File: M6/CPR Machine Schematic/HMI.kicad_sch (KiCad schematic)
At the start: 0 parts

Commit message: morer kicad
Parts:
- added J2: Raspberry_Pi_4, symbol Connector:Raspberry_Pi_4
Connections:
- new net: J2.1 (3V3), J2.17 (3V3)
- new net: J2.14 (GND), J2.20 (GND), J2.25 (GND), J2.30 (GND), J2.34 (GND), J2.39 (GND), J2.6 (GND), J2.9 (GND)
- new net +5V: J2.2 (5V), J2.4 (5V)
- new net UART_RX: J2.10 (GPIO15/UART_RXD)
- new net UART_TX: J2.8 (GPIO14/UART_TXD)
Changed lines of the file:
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@@
 	(generator_version "9.0")
 	(paper "A4")
+	(hierarchical_label "UART_TX"
+		(shape output)
+		(at 48.26 68.58 180)
+		(effects
+			(font
+				(size 1.27 1.27)
+			)
+			(justify right)
+		)
+	)
+	(hierarchical_label "UART_RX"
+		(shape input)
+		(at 48.26 71.12 180)
+		(effects
+			(font
+				(size 1.27 1.27)
+			)
+			(justify right)
+		)
+	)
+	(symbol
+		(lib_id "power:+5V")
+		(at 114.3 60.96 270)
+		(unit 1)
+		(exclude_from_sim no)
+		(in_bom yes)
+		(on_board yes)
+		(dnp no)
+		(fields_autoplaced yes)
+		(property "Reference" "#PWR02"
+			(at 110.49 60.96 0)
+			(effects
+				(font
+					(size 1.27 1.27)
+				)
+				(hide yes)
+			)
+		)
+		(property "Value" "+5V"
+			(at 118.11 60.9599 90)
+			(effects
+				(font
+					(size 1.27 1.27)
+				)
+				(justify left)
+			)
+		)
+		(property "Footprint" ""
+			(at 114.3 60.96 0)
+			(effects
+				(font
+					(size 1.27 1.27)
+				)
+				(hide yes)
+			)
+		)
+		(property "Datasheet" ""
+			(at 114.3 60.96 0)
+			(effects
+				(font
+					(size 1.27 1.27)
+				)
+				(hide yes)
+			)
+		)
+		(property "Description" "Power symbol creates a global label with name \"+5V\""
+			(at 114.3 60.96 0)
+			(effects
+				(font
+					(size 1.27 1.27)
+				)
+				(hide yes)
+			)
+		)
+		(pin "1"
+		)
+		(instances
+			(project ""
+				(path "/8991fc77-975f-4978-a089-6b2a5e33f59b/6f4ed3f2-e76d-4623-90c5-067eb820b8e2"
+					(reference "#PWR02")
+					(unit 1)
+				)
+			)
+		)
+	)
+	(symbol
+		(lib_id "Connector:Raspberry_Pi_4")
+		(at 81.28 83.82 0)
+		(unit 1)
+		(exclude_from_sim no)
+		(in_bom yes)
+		(on_board yes)
+		(dnp no)
+		(fields_autoplaced yes)
+		(property "Reference" "J2"
+			(at 81.28 53.34 0)
+			(effects
+				(font
+					(size 1.27 1.27)
+				)
+			)
+		)
+		(property "Value" "Raspberry_Pi_4"
+			(at 81.28 55.88 0)
+			(effects
+				(font
+					(size 1.27 1.27)
+				)
+			)
+		)
+		(property "Footprint" ""
+			(at 151.384 131.318 0)
+			(effects
+				(font
+					(size 1.27 1.27)
+				)
+				(justify left)
+				(hide yes)
+			)
+		)
+		(property "Datasheet" "https://datasheets.raspberrypi.com/rpi4/raspberry-pi-4-datasheet.pdf"
+			(at 97.028 116.078 0)
+			(effects
+				(font
+					(size 1.27 1.27)
+				)
+				(justify left)
+				(hide yes)
+			)
+		)
+		(property "Description" "Raspberry Pi 4 Model B"
+			(at 97.028 113.538 0)
+			(effects
+				(font
+					(size 1.27 1.27)
+				)
+				(justify left)
+				(hide yes)
+			)
+		)
+		(pin "32"
+		)
+		(pin "33"
+		)
+		(pin "35"
+		)
+		(pin "22"
+		)
+		(pin "20"
+		)
+		(pin "25"
+		)
+		(pin "30"
+		)
+		(pin "8"
+		)
+		(pin "6"
+		)
+		(pin "40"
+		)
+		(pin "12"
+		)
+		(pin "14"
+		)
+		(pin "13"
+		)
+		(pin "36"
+		)
+		(pin "38"
+		)
+		(pin "10"
+		)
+		(pin "15"
+		)
+		(pin "34"
+		)
+		(pin "16"
+		)
+		(pin "18"
+		)
+		(pin "39"
+		)
+		(pin "37"
+		)
+		(pin "11"
+		)
+		(pin "31"
+		)
+		(pin "5"
+		)
+		(pin "9"
+		)
+		(pin "17"
+		)
+		(pin "1"
+		)
+		(pin "21"
+		)
+		(pin "19"
+		)
+		(pin "27"
+		)
+		(pin "7"
+		)
+		(pin "4"
+		)
+		(pin "29"
+		)
+		(pin "23"
+		)
+		(pin "3"
+		)
+		(pin "2"
+		)
+		(pin "28"
+		)
+		(pin "26"
+		)
+		(pin "24"
+		)
+		(instances
+			(project ""
+				(path "/8991fc77-975f-4978-a089-6b2a5e33f59b/6f4ed3f2-e76d-4623-90c5-067eb820b8e2"
+					(reference "J2")
+					(unit 1)
+				)
+			)
+		)
+	)
 )

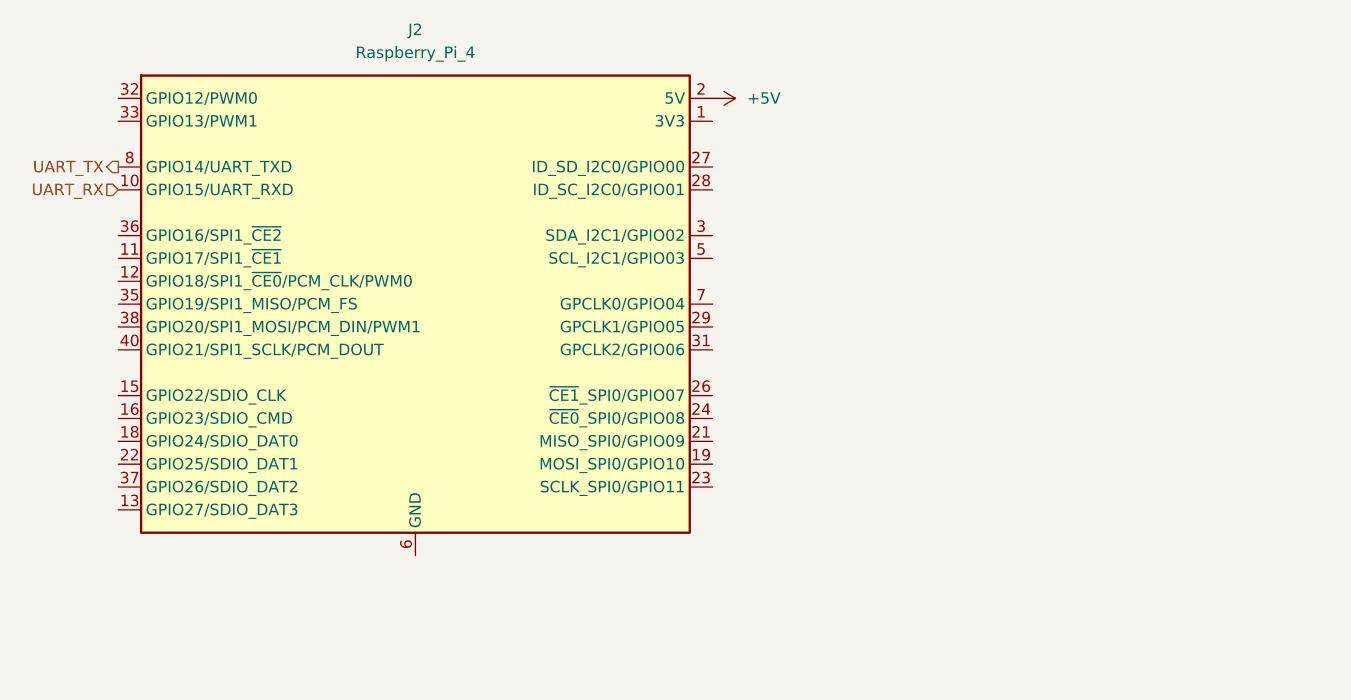
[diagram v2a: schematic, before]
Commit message: HMI Raspi
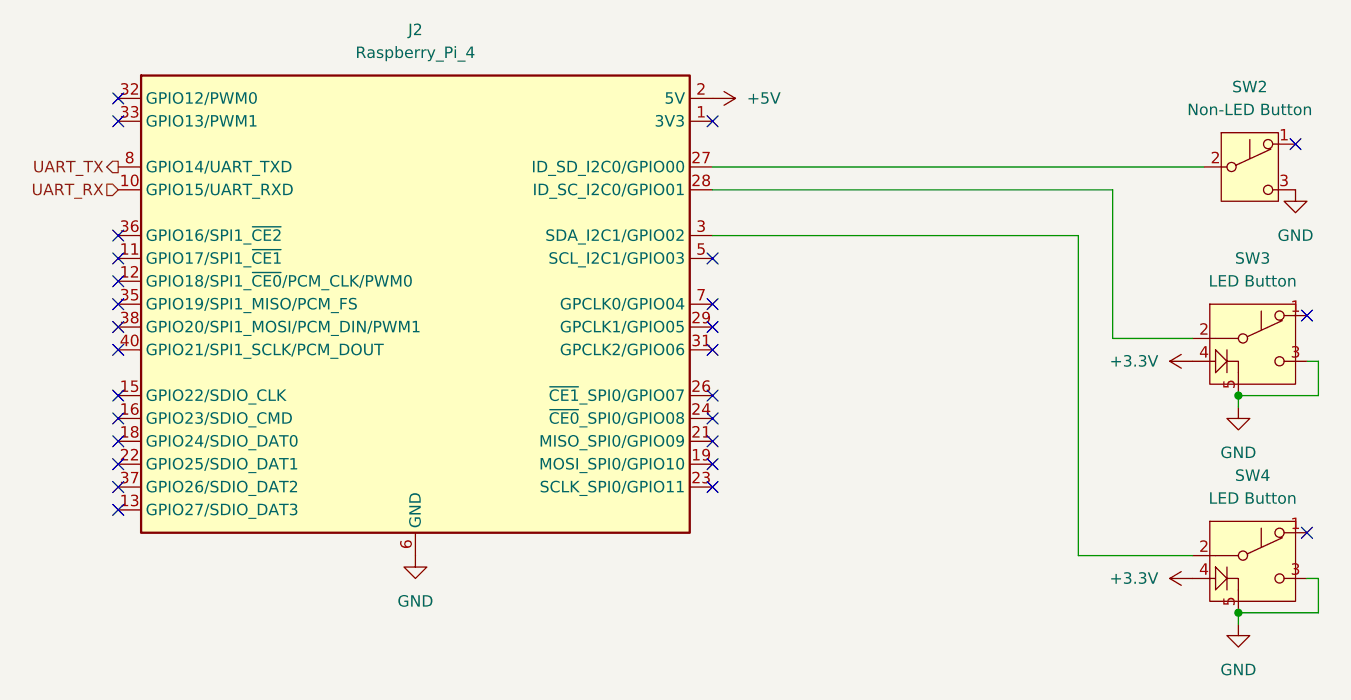
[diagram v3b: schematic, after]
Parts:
- added SW2: Non-LED Button, symbol Switch:SW_Push_SPDT
- added SW3, SW4: LED Button, symbol Switch:SW_Push_SPDT
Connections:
- net GND: now reaches J2.14 (GND), J2.20 (GND), J2.25 (GND), J2.30 (GND), J2.34 (GND), J2.39 (GND), J2.6 (GND), J2.9 (GND)
- net GND: now also SW2.3 (C), SW3.3 (C), SW3.5 (GND), SW4.3 (C), SW4.5 (GND)
- net at J2.27 (ID_SD_I2C0/GPIO00): now also SW2.2 (B)
- net at J2.28 (ID_SC_I2C0/GPIO01): now also SW3.2 (B)
- net at J2.3 (SDA_I2C1/GPIO02): now also SW4.2 (B)
- new net +3.3V: SW3.4 (LED_IN), SW4.4 (LED_IN)
- no-connect marks 0 -> 27

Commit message: HMI schem for real for real
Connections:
- net at J2.3 (SDA_I2C1/GPIO02): now also SW3.4 (LED_IN); no longer SW4.2 (B)
- net at J2.5 (SCL_I2C1/GPIO03): now also SW4.2 (B)
- net at J2.7 (GPCLK0/GPIO04): now also SW4.4 (LED_IN)
- removed net +3.3V: SW3.4 (LED_IN), SW4.4 (LED_IN)
- no-connect marks 27 -> 25
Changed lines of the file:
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@@
-	)
-	(no_connect
-		(at 114.3 78.74)
 	)
 	(no_connect
@@
 	)
 	(no_connect
-		(at 114.3 83.82)
-	)
-	(no_connect
 		(at 180.34 85.09)
 	)
@@
 	(wire
 		(pts
+			(xy 151.13 114.3) (xy 151.13 83.82)
+		)
+		(stroke
+			(width 0)
+			(type default)
+		)
+	)
+	(wire
+		(pts
+			(xy 167.64 114.3) (xy 151.13 114.3)
+		)
+		(stroke
+			(width 0)
+			(type default)
+		)
+	)
+	(wire
+		(pts
+			(xy 151.13 83.82) (xy 114.3 83.82)
+		)
+		(stroke
+			(width 0)
+			(type default)
+		)
+	)
+	(wire
+		(pts
+			(xy 114.3 76.2) (xy 156.21 76.2)
+		)
+		(stroke
+			(width 0)
+			(type default)
+		)
+	)
+	(wire
+		(pts
 			(xy 114.3 71.12) (xy 158.75 71.12)
 		)
@@
 	(wire
 		(pts
-			(xy 154.94 111.76) (xy 167.64 111.76)
-		)
-		(stroke
-			(width 0)
-			(type default)
-		)
-	)
-	(wire
-		(pts
 			(xy 181.61 114.3) (xy 181.61 118.11)
 		)
@@
 	(wire
 		(pts
+			(xy 114.3 78.74) (xy 153.67 78.74)
+		)
+		(stroke
+			(width 0)
+			(type default)
+		)
+	)
+	(wire
+		(pts
 			(xy 180.34 114.3) (xy 181.61 114.3)
 		)
@@
 	(wire
 		(pts
+			(xy 153.67 111.76) (xy 167.64 111.76)
+		)
+		(stroke
+			(width 0)
+			(type default)
+		)
+	)
+	(wire
+		(pts
 			(xy 181.61 93.98) (xy 172.72 93.98)
 		)
@@
 	(wire
 		(pts
+			(xy 156.21 90.17) (xy 156.21 76.2)
+		)
+		(stroke
+			(width 0)
+			(type default)
+		)
+	)
+	(wire
+		(pts
+			(xy 153.67 78.74) (xy 153.67 111.76)
+		)
+		(stroke
+			(width 0)
+			(type default)
+		)
+	)
+	(wire
+		(pts
 			(xy 114.3 68.58) (xy 168.91 68.58)
 		)
@@
 	(wire
 		(pts
-			(xy 154.94 111.76) (xy 154.94 76.2)
+			(xy 167.64 90.17) (xy 156.21 90.17)
 		)
 		(stroke
@@
 		(pts
 			(xy 181.61 90.17) (xy 181.61 93.98)
-		)
-		(stroke
-			(width 0)
-			(type default)
-		)
-	)
-	(wire
-		(pts
-			(xy 154.94 76.2) (xy 114.3 76.2)
 		)
 		(stroke
@@
 	)
 	(symbol
-		(lib_id "power:+3.3V")
-		(at 167.64 114.3 90)
-		(unit 1)
-		(exclude_from_sim no)
-		(in_bom yes)
-		(on_board yes)
-		(dnp no)
-		(fields_autoplaced yes)
-		(property "Reference" "#PWR029"
-			(at 171.45 114.3 0)
-			(effects
-				(font
-					(size 1.27 1.27)
-				)
-				(hide yes)
-			)
-		)
-		(property "Value" "+3.3V"
-			(at 163.83 114.2999 90)
-			(effects
-				(font
-					(size 1.27 1.27)
-				)
-				(justify left)
-			)
-		)
-		(property "Footprint" ""
-			(at 167.64 114.3 0)
-			(effects
-				(font
-					(size 1.27 1.27)
-				)
-				(hide yes)
-			)
-		)
-		(property "Datasheet" ""
-			(at 167.64 114.3 0)
-			(effects
-				(font
-					(size 1.27 1.27)
-				)
-				(hide yes)
-			)
-		)
-		(property "Description" "Power symbol creates a global label with name \"+3.3V\""
-			(at 167.64 114.3 0)
-			(effects
-				(font
-					(size 1.27 1.27)
-				)
-				(hide yes)
-			)
-		)
-		(pin "1"
-		)
-		(instances
-			(project "CPR Machine Schematic"
-				(path "/8991fc77-975f-4978-a089-6b2a5e33f59b/6f4ed3f2-e76d-4623-90c5-067eb820b8e2"
-					(reference "#PWR029")
-					(unit 1)
-				)
-			)
-		)
-	)
-	(symbol
 		(lib_id "power:GND")
 		(at 81.28 111.76 0)
@@
 					(unit 1)
 				)
-			)
-		)
-	)
-	(symbol
-		(lib_id "power:+3.3V")
-		(at 167.64 90.17 90)
-		(unit 1)
-		(exclude_from_sim no)
-		(in_bom yes)
-		(on_board yes)
-		(dnp no)
-		(fields_autoplaced yes)
-		(property "Reference" "#PWR028"
-			(at 171.45 90.17 0)
-			(effects
-				(font
-					(size 1.27 1.27)
-				)
-				(hide yes)
-			)
-		)
-		(property "Value" "+3.3V"
-			(at 163.83 90.1699 90)
-			(effects
-				(font
-					(size 1.27 1.27)
-				)
-				(justify left)
-			)
-		)
-		(property "Footprint" ""
-			(at 167.64 90.17 0)
-			(effects
-				(font
-					(size 1.27 1.27)
-				)
-				(hide yes)
-			)
-		)
-		(property "Datasheet" ""
-			(at 167.64 90.17 0)
-			(effects
-				(font
-					(size 1.27 1.27)
-				)
-				(hide yes)
-			)
-		)
-		(property "Description" "Power symbol creates a global label with name \"+3.3V\""
-			(at 167.64 90.17 0)
-			(effects
-				(font
-					(size 1.27 1.27)
-				)
-				(hide yes)
-			)
-		)
-		(pin "1"
-		)
-		(instances
-			(project ""
-				(path "/8991fc77-975f-4978-a089-6b2a5e33f59b/6f4ed3f2-e76d-4623-90c5-067eb820b8e2"
-					(reference "#PWR028")
-					(unit 1)
-				)
